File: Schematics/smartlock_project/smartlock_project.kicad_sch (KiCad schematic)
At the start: 11 parts, among them U1 ESP-12E

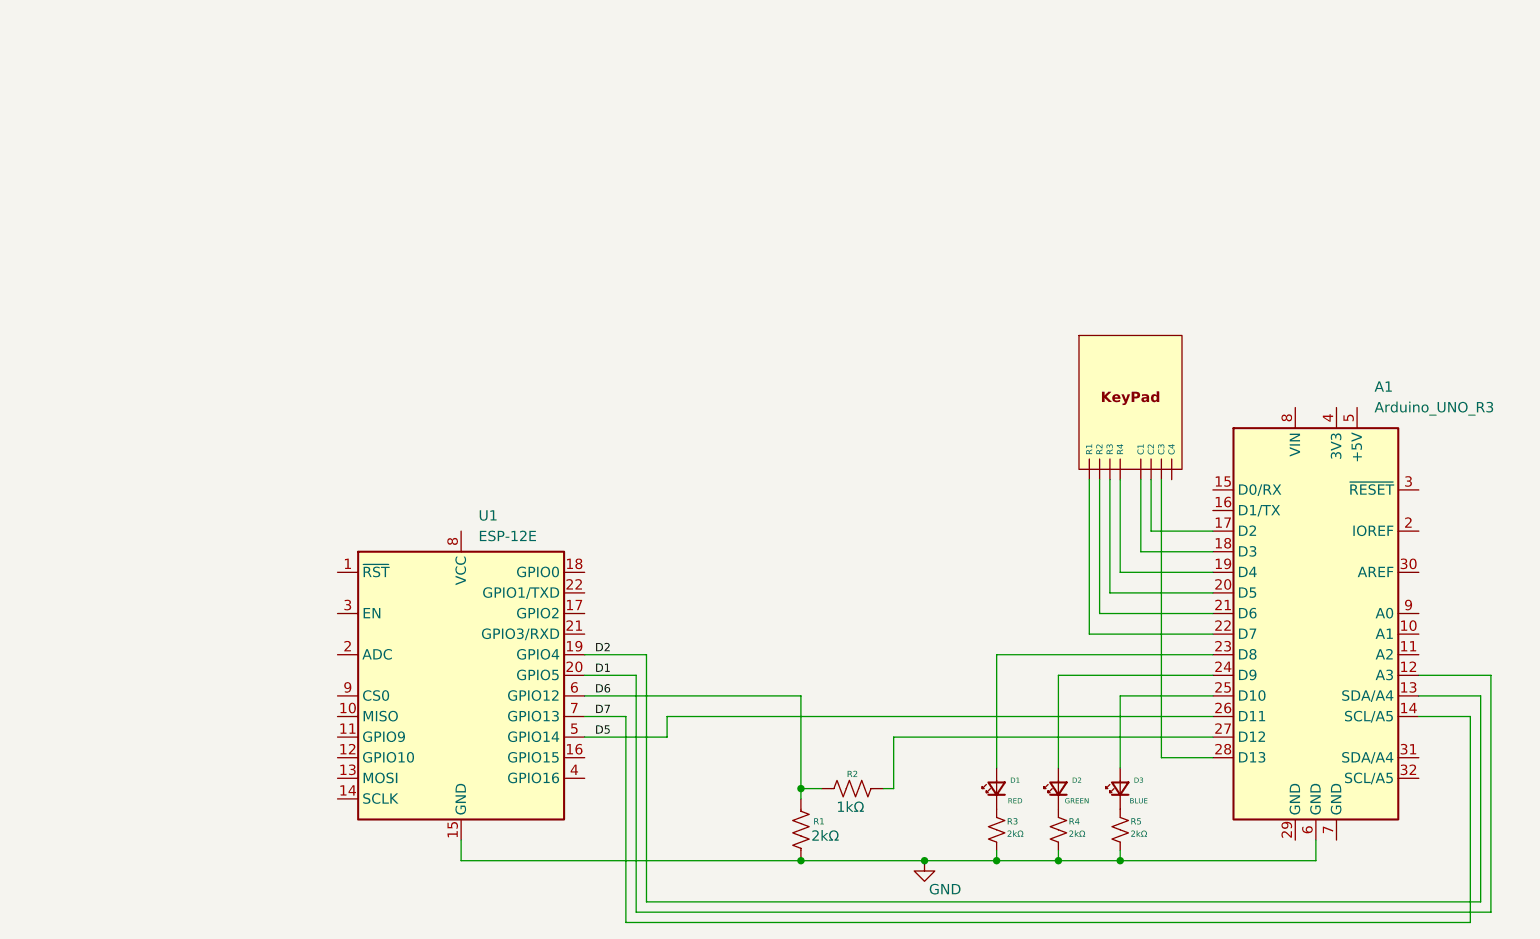
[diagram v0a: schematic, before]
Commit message: 1.0.2 - Added Architecture diagram xml
- Created the architecture diagram xml with draw.io.
- Fixed the page layout in the wiring schematics.
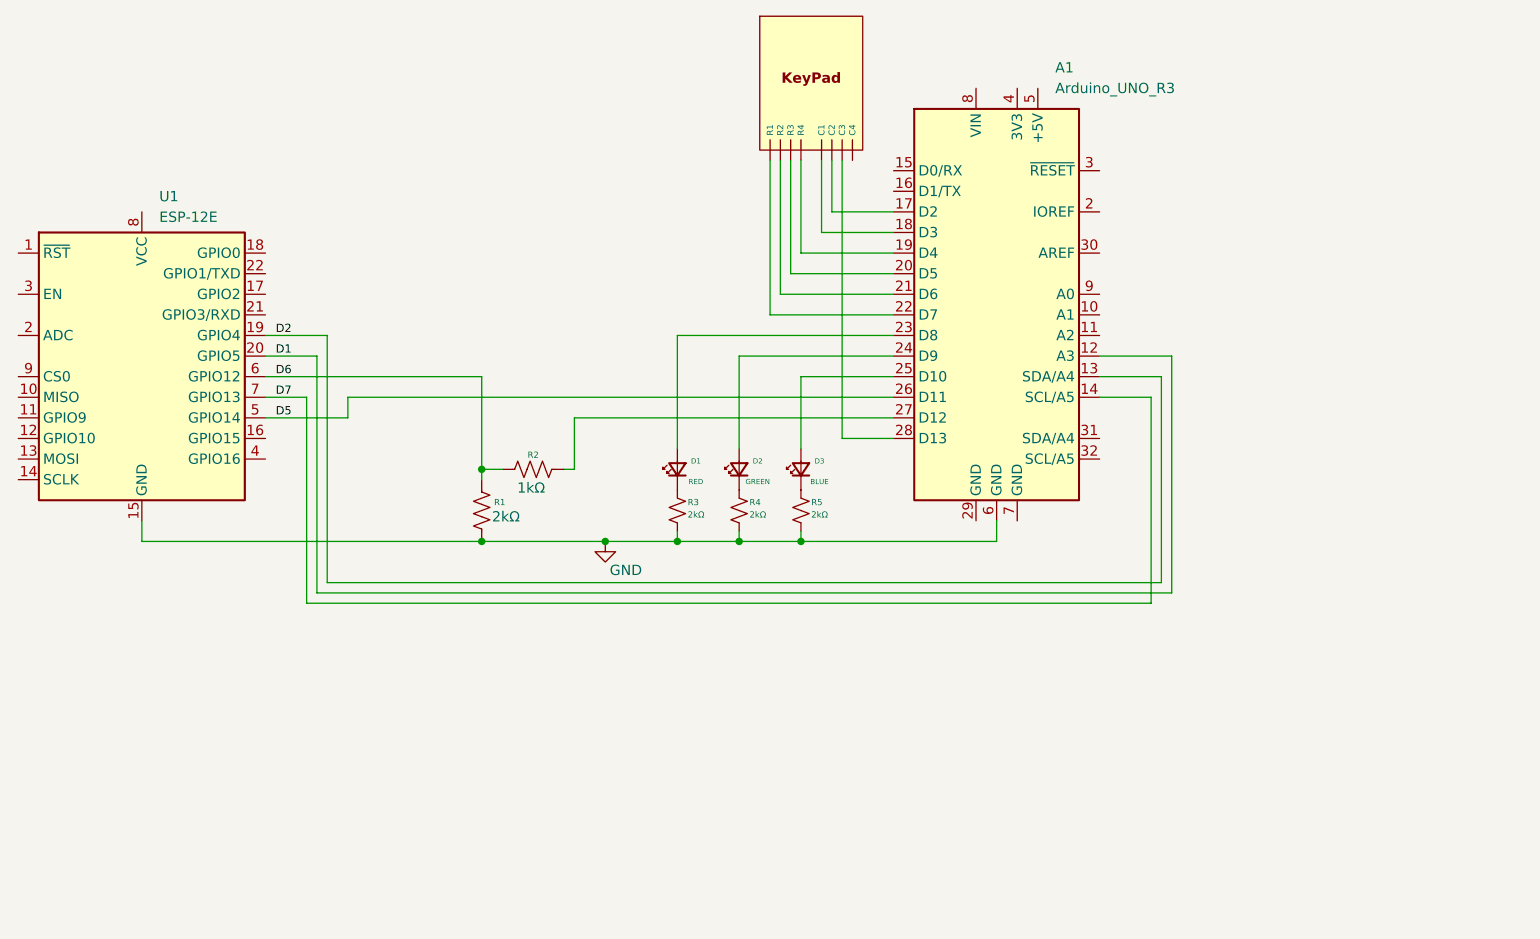
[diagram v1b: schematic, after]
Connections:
- net at KeyPad1. (C4): now also A1.28 (D13)
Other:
- moved on the sheet: A1, D1, D2, D3, R1, R2, R3, R4, R5, U1
